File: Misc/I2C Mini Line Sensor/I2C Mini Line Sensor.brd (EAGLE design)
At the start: 33 x 12.7 mm, 16 parts, among them U1 ADS1015.RUG, U2 QRE1113, U3 QRE1113, U4 QRE1113, U5 QRE1113

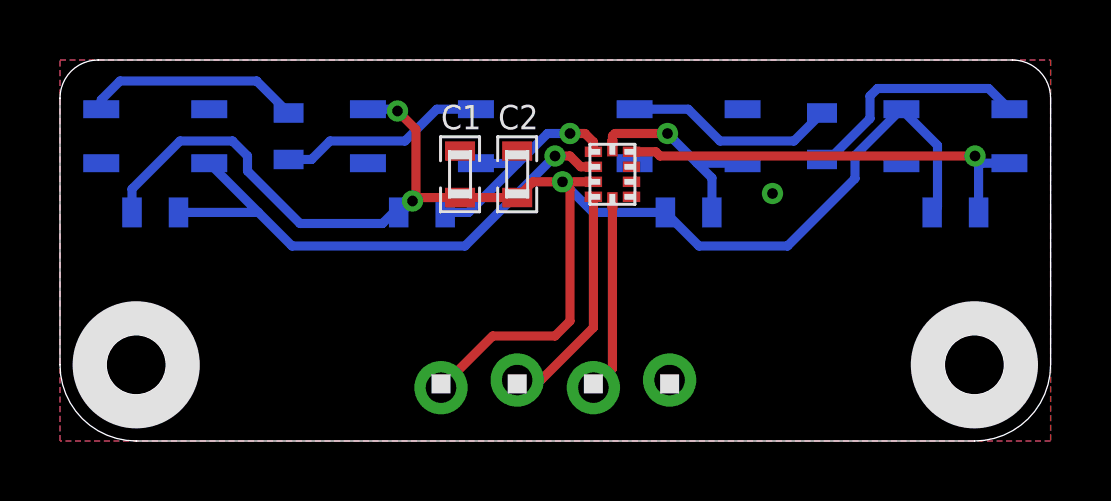
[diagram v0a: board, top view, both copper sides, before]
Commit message: Added address select pins for IC
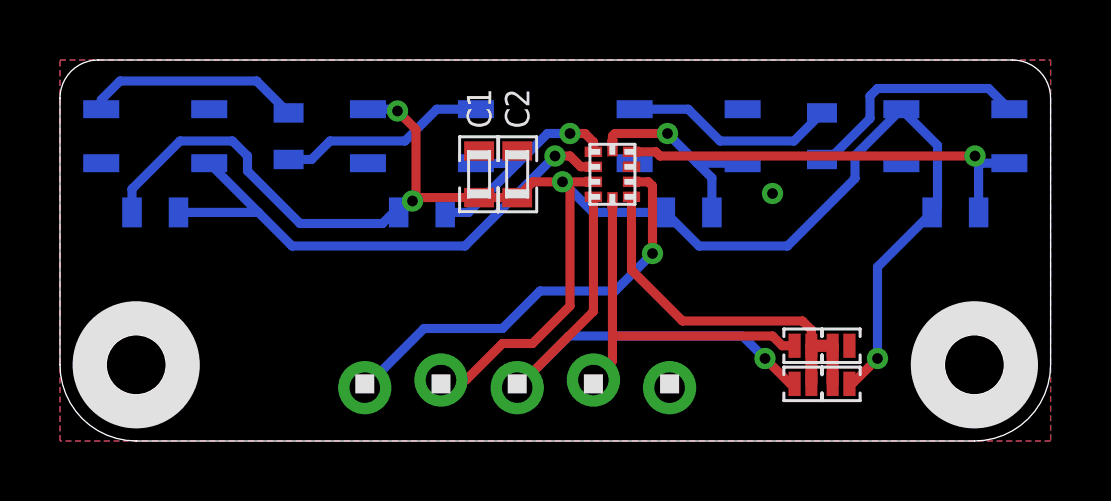
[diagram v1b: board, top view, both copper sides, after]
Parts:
- removed U$6: 1X4.LOCK, headers(.1in):1X4.LOCK
- added J1, J2, J3, J4: (no value), solderjumper:2.MED
- added U$21: 1X5.LOCK, headers(.1in):1X5.LOCK
- moved C1 0.63 mm to (14.0, 8.89)
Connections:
- net 3.3V: now also J3.2, U$21.2; no longer U$6.1
- net ADDR: now also J1.1, J2.1, J3.1, J4.1
- net GND: now also J4.2, U$21.5; no longer U$6.4
- net RDY: now also U$21.1
- net SCL: now also J1.2, U$21.4; no longer U$6.3
- net SDA: now also J2.2, U$21.3; no longer U$6.2
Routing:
- net RDY: track 0.00 -> 14.5 mm, vias 0 -> 1
- net ADDR: track 0.00 -> 13.0 mm
- net SDA: track 7.62 -> 18.0 mm, vias 0 -> 1
- net 3.3V: track 51.5 -> 58.0 mm, vias 3 -> 4
- net SCL: track 6.49 -> 12.4 mm
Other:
- board text added: "RDY"
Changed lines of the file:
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@@
 <setting verticaltext="up"/>
 </settings>
-<grid distance="25" unitdist="mil" unit="mil" style="dots" multiple="2" display="yes" altdistance="5" altunitdist="mil" altunit="mil"/>
+<grid distance="0.25" unitdist="mm" unit="mm" style="dots" multiple="2" display="yes" altdistance="0.05" altunitdist="mm" altunit="mm"/>
 <layers>
 <layer number="1" name="Top" color="4" fill="1" visible="yes" active="yes"/>
@@
 <text x="25.4" y="0.635" size="0.8128" layer="52" ratio="12" rot="MR0" align="bottom-center">Cruz
 Monrreal II</text>
-<text x="7.62" y="0.635" size="0.8128" layer="52" ratio="12" rot="MR0" align="bottom-center">Anomalous
+<text x="7.62" y="3.175" size="0.8128" layer="52" ratio="12" rot="MR0" align="bottom-center">Anomalous
 Maker.com</text>
 <text x="16.51" y="5.715" size="1.27" layer="51" ratio="12" align="bottom-center">I2C Mini Line Sensor</text>
@@
 <wire x1="20.32" y1="10.16" x2="21.59" y2="10.16" width="0.1524" layer="51"/>
 <wire x1="29.21" y1="10.16" x2="30.48" y2="10.16" width="0.1524" layer="51"/>
+<text x="8.89" y="1.905" size="0.8128" layer="52" ratio="12" rot="MR0" align="center-left">RDY</text>
+<text x="8.89" y="1.905" size="0.8128" layer="51" ratio="12" rot="R180" align="center-left">RDY</text>
 </plain>
 <attributes>
@@
 </autorouter>
 <elements>
-<element name="C1" library="standardparts" package="0603" value=".1uF" x="13.335" y="8.89" smashed="yes" rot="R90">
-<attribute name="NAME" x="12.7" y="10.795" size="0.8128" layer="25" font="vector" ratio="12" align="center-left"/>
+<element name="C1" library="standardparts" package="0603" value=".1uF" x="13.97" y="8.89" smashed="yes" rot="R90">
+<attribute name="NAME" x="13.97" y="10.414" size="0.8128" layer="25" font="vector" ratio="12" rot="R90" align="center-left"/>
 </element>
 <element name="C2" library="standardparts" package="0603" value="1uF" x="15.24" y="8.89" smashed="yes" rot="R90">
-<attribute name="NAME" x="14.605" y="10.795" size="0.8128" layer="25" font="vector" ratio="12" align="center-left"/>
-</element>
-<element name="U$6" library="headers(.1in)" package="1X4.LOCK" value="1X4.LOCK" x="12.7" y="1.905"/>
+<attribute name="NAME" x="15.24" y="10.414" size="0.8128" layer="25" font="vector" ratio="12" rot="R90" align="center-left"/>
+</element>
 <element name="U1" library="packages(ti)" package="RUG.10" value="ADS1015.RUG" x="18.415" y="8.89" smashed="yes" rot="R180"/>
 <element name="U$3" library="screw_holes" package="2MM" value="HOLE.2MM" x="2.54" y="2.54"/>
@@
 <attribute name="NAME" x="8.255" y="8.255" size="0.8128" layer="26" font="vector" ratio="12" rot="MR0" align="center-left"/>
 </element>
+<element name="J1" library="solderjumper" package="2.MED" value="" x="24.765" y="3.175" smashed="yes" rot="R180">
+<attribute name="VALUE" x="25.515" y="4.425" size="0.4064" layer="27" rot="R180"/>
+</element>
+<element name="J2" library="solderjumper" package="2.MED" value="" x="24.765" y="1.905" smashed="yes" rot="R180">
+<attribute name="VALUE" x="25.515" y="3.155" size="0.4064" layer="27" rot="R180"/>
+</element>
+<element name="J3" library="solderjumper" package="2.MED" value="" x="26.035" y="1.905" smashed="yes">
+<attribute name="VALUE" x="25.285" y="0.655" size="0.4064" layer="27"/>
+</element>
+<element name="J4" library="solderjumper" package="2.MED" value="" x="26.035" y="3.175" smashed="yes">
+<attribute name="VALUE" x="25.285" y="1.925" size="0.4064" layer="27"/>
+</element>
+<element name="U$21" library="headers(.1in)" package="1X5.LOCK" value="1X5.LOCK" x="10.16" y="1.905"/>
 </elements>
 <signals>
@@
 <contactref element="C1" pad="2"/>
 <contactref element="C2" pad="2"/>
-<contactref element="U$6" pad="4"/>
 <contactref element="U1" pad="3"/>
 <contactref element="U5" pad="2"/>
@@
 <contactref element="U5" pad="4"/>
 <via x="23.75" y="8.25" extent="1-16" drill="0.3556"/>
+<contactref element="J4" pad="2"/>
+<contactref element="U$21" pad="5"/>
 </signal>
 <signal name="SDA">
-<contactref element="U$6" pad="2"/>
 <contactref element="U1" pad="9"/>
-<wire x1="17.78" y1="8.14" x2="17.78" y2="3.78" width="0.3048" layer="1"/>
-<wire x1="17.78" y1="3.78" x2="16.032" y2="2.032" width="0.3048" layer="1"/>
-<wire x1="16.032" y1="2.032" x2="15.24" y2="2.032" width="0.3048" layer="1"/>
+<wire x1="17.78" y1="8.14" x2="17.78" y2="4.318" width="0.3048" layer="1"/>
+<contactref element="J2" pad="2"/>
+<via x="23.5" y="2.75" extent="1-16" drill="0.3556"/>
+<wire x1="23.5" y1="2.75" x2="22.75" y2="3.5" width="0.3048" layer="16"/>
+<wire x1="22.75" y1="3.5" x2="16.962" y2="3.5" width="0.3048" layer="16"/>
+<wire x1="23.5" y1="2.75" x2="24.345" y2="1.905" width="0.3048" layer="1"/>
+<wire x1="24.345" y1="1.905" x2="24.4856" y2="1.905" width="0.3048" layer="1"/>
+<contactref element="U$21" pad="3"/>
+<wire x1="17.78" y1="4.318" x2="15.24" y2="1.778" width="0.3048" layer="1"/>
+<wire x1="16.962" y1="3.5" x2="15.24" y2="1.778" width="0.3048" layer="16"/>
 </signal>
 <signal name="SCL">
-<contactref element="U$6" pad="3"/>
 <contactref element="U1" pad="10"/>
-<wire x1="18.415" y1="8.005" x2="18.415" y2="2.413" width="0.3048" layer="1"/>
-<wire x1="18.415" y1="2.413" x2="17.78" y2="1.778" width="0.3048" layer="1"/>
+<wire x1="18.415" y1="8.005" x2="18.415" y2="3.5" width="0.3048" layer="1"/>
+<contactref element="J1" pad="2"/>
+<wire x1="24.4856" y1="3.175" x2="24.075" y2="3.175" width="0.3048" layer="1"/>
+<wire x1="24.075" y1="3.175" x2="23.75" y2="3.5" width="0.3048" layer="1"/>
+<wire x1="23.75" y1="3.5" x2="18.415" y2="3.5" width="0.3048" layer="1"/>
+<contactref element="U$21" pad="4"/>
+<wire x1="18.415" y1="3.5" x2="18.415" y2="2.667" width="0.3048" layer="1"/>
+<wire x1="18.415" y1="2.667" x2="17.78" y2="2.032" width="0.3048" layer="1"/>
 </signal>
 <signal name="D">
@@
 <contactref element="C1" pad="1"/>
 <contactref element="C2" pad="1"/>
-<contactref element="U$6" pad="1"/>
 <contactref element="U1" pad="8"/>
 <contactref element="R1" pad="1"/>
@@
 <wire x1="6.25" y1="9.5" x2="6.25" y2="9" width="0.3048" layer="16"/>
 <wire x1="6.25" y1="9" x2="8" y2="7.25" width="0.3048" layer="16"/>
-<wire x1="13.335" y1="8.115" x2="15.24" y2="8.115" width="0.3048" layer="1"/>
+<wire x1="13.97" y1="8.115" x2="15.24" y2="8.115" width="0.3048" layer="1"/>
 <wire x1="17.78" y1="8.64" x2="16.75" y2="8.64" width="0.3048" layer="1"/>
 <wire x1="15.765" y1="8.64" x2="15.24" y2="8.115" width="0.3048" layer="1"/>
-<wire x1="13.335" y1="8.115" x2="11.865" y2="8.115" width="0.3048" layer="1"/>
+<wire x1="13.97" y1="8.115" x2="11.865" y2="8.115" width="0.3048" layer="1"/>
 <wire x1="11.865" y1="8.115" x2="11.75" y2="8" width="0.3048" layer="1"/>
 <via x="11.75" y="8" extent="1-16" drill="0.3556"/>
@@
 <via x="16.75" y="8.64" extent="1-16" drill="0.3556"/>
 <wire x1="16.75" y1="8.64" x2="15.765" y2="8.64" width="0.3048" layer="1"/>
-<wire x1="12.7" y1="1.778" x2="14.422" y2="3.5" width="0.3048" layer="1"/>
-<wire x1="14.422" y1="3.5" x2="16.5" y2="3.5" width="0.3048" layer="1"/>
-<wire x1="16.5" y1="3.5" x2="17" y2="4" width="0.3048" layer="1"/>
-<wire x1="17" y1="4" x2="17" y2="8.39" width="0.3048" layer="1"/>
-<wire x1="17" y1="8.39" x2="16.75" y2="8.64" width="0.3048" layer="1"/>
 <wire x1="8" y1="7.25" x2="10.75" y2="7.25" width="0.3048" layer="16"/>
 <wire x1="10.75" y1="7.25" x2="11.12" y2="7.62" width="0.3048" layer="16"/>
 <wire x1="11.12" y1="7.62" x2="11.29" y2="7.62" width="0.3048" layer="16"/>
+<contactref element="J3" pad="2"/>
+<via x="27.25" y="2.75" extent="1-16" drill="0.3556"/>
+<wire x1="27.25" y1="2.75" x2="27.25" y2="5.8" width="0.3048" layer="16"/>
+<wire x1="27.25" y1="5.8" x2="29.07" y2="7.62" width="0.3048" layer="16"/>
+<wire x1="26.3144" y1="1.905" x2="26.405" y2="1.905" width="0.3048" layer="1"/>
+<wire x1="26.405" y1="1.905" x2="27.25" y2="2.75" width="0.3048" layer="1"/>
+<contactref element="U$21" pad="2"/>
+<wire x1="16.75" y1="8.64" x2="17" y2="8.39" width="0.3048" layer="1"/>
+<wire x1="17" y1="8.39" x2="17" y2="4.5" width="0.3048" layer="1"/>
+<wire x1="17" y1="4.5" x2="15.75" y2="3.25" width="0.3048" layer="1"/>
+<wire x1="15.75" y1="3.25" x2="14.75" y2="3.25" width="0.3048" layer="1"/>
+<wire x1="14.75" y1="3.25" x2="13.532" y2="2.032" width="0.3048" layer="1"/>
+<wire x1="13.532" y1="2.032" x2="12.7" y2="2.032" width="0.3048" layer="1"/>
 </signal>
 <signal name="ADDR">
 <contactref element="U1" pad="1"/>
+<contactref element="J1" pad="1"/>
+<contactref element="J2" pad="1"/>
+<contactref element="J3" pad="1"/>
+<contactref element="J4" pad="1"/>
+<wire x1="25.0444" y1="3.175" x2="25.7556" y2="3.175" width="0.4064" layer="1"/>
+<wire x1="25.7556" y1="1.905" x2="25.7556" y2="3.175" width="0.4064" layer="1"/>
+<wire x1="25.0444" y1="1.905" x2="25.0444" y2="3.175" width="0.4064" layer="1"/>
+<wire x1="19.05" y1="8.14" x2="19.05" y2="5.7" width="0.3048" layer="1"/>
+<wire x1="19.05" y1="5.7" x2="20.75" y2="4" width="0.3048" layer="1"/>
+<wire x1="20.75" y1="4" x2="24.75" y2="4" width="0.3048" layer="1"/>
+<wire x1="24.75" y1="4" x2="25.0444" y2="3.7056" width="0.3048" layer="1"/>
+<wire x1="25.0444" y1="3.7056" x2="25.0444" y2="3.175" width="0.3048" layer="1"/>
 </signal>
 <signal name="RDY">
 <contactref element="U1" pad="2"/>
+<wire x1="19.05" y1="8.64" x2="19.61" y2="8.64" width="0.3048" layer="1"/>
+<wire x1="19.61" y1="8.64" x2="19.75" y2="8.5" width="0.3048" layer="1"/>
+<wire x1="19.75" y1="8.5" x2="19.75" y2="6.25" width="0.3048" layer="1"/>
+<via x="19.75" y="6.25" extent="1-16" drill="0.3556"/>
+<wire x1="19.75" y1="6.25" x2="18.5" y2="5" width="0.3048" layer="16"/>
+<contactref element="U$21" pad="1"/>
+<wire x1="18.5" y1="5" x2="16" y2="5" width="0.3048" layer="16"/>
+<wire x1="16" y1="5" x2="14.75" y2="3.75" width="0.3048" layer="16"/>
+<wire x1="14.75" y1="3.75" x2="12.132" y2="3.75" width="0.3048" layer="16"/>
+<wire x1="12.132" y1="3.75" x2="10.16" y2="1.778" width="0.3048" layer="16"/>
 </signal>
 <signal name="N$1">
@@
 </signal>
 </signals>
-<errors>
-</errors>
 </board>
 </drawing>

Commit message: Cleaned up layout of I2C Mini Line Sensor and I2C Line Sensor Also geenerated preview images
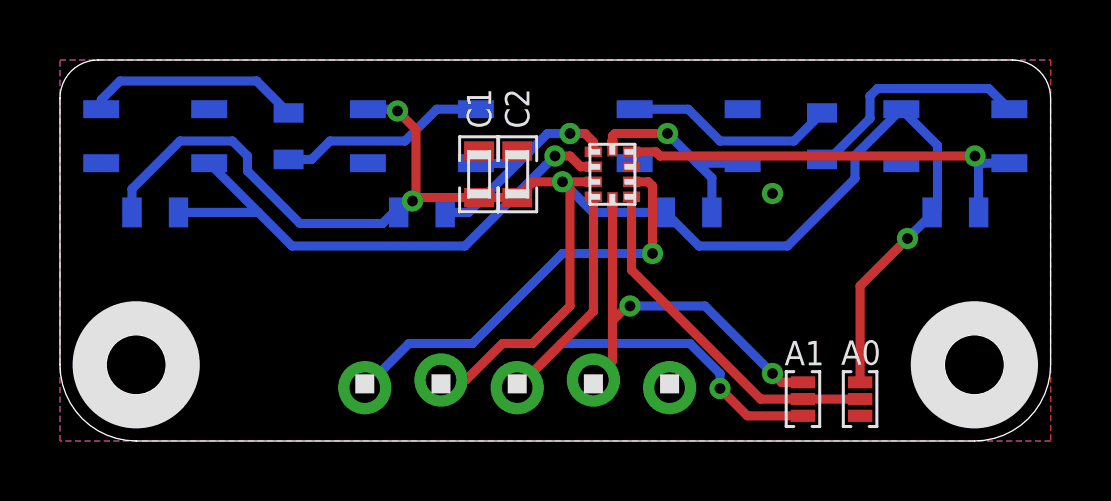
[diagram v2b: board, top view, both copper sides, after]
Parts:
- removed J1, J2, J3, J4: (no value), solderjumper:2.MED
- added A0, A1: (no value), solderjumper:3.MED
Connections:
- net 3.3V: now also A0.1; no longer J3.2
- net ADDR: now also A0.2, A1.2; no longer J1.1, J2.1, J3.1, J4.1
- net GND: now also A0.3; no longer J4.2
- net SCL: now also A1.1; no longer J1.2
- net SDA: now also A1.3; no longer J2.2
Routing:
- net SCL: track 12.4 -> 13.8 mm, vias 0 -> 2
- net ADDR: track 13.0 -> 11.8 mm
- net SDA: track 18.0 -> 18.8 mm

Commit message: Modified resistor values such that the PCBs should no longer get hot
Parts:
- R5, R6: value 33 -> 51
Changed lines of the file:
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@@
 <attribute name="NAME" x="1.27" y="8.509" size="0.8128" layer="26" font="vector" ratio="12" rot="MR270" align="center-left"/>
 </element>
-<element name="R5" library="standardparts" package="0603" value="33" x="25.4" y="10.16" smashed="yes" rot="MR90">
+<element name="R5" library="standardparts" package="0603" value="51" x="25.4" y="10.16" smashed="yes" rot="MR90">
 <attribute name="NAME" x="26.035" y="8.255" size="0.8128" layer="26" font="vector" ratio="12" rot="MR0" align="center-left"/>
 </element>
-<element name="R6" library="standardparts" package="0603" value="33" x="7.62" y="10.16" smashed="yes" rot="MR90">
+<element name="R6" library="standardparts" package="0603" value="51" x="7.62" y="10.16" smashed="yes" rot="MR90">
 <attribute name="NAME" x="8.255" y="8.255" size="0.8128" layer="26" font="vector" ratio="12" rot="MR0" align="center-left"/>
 </element>
